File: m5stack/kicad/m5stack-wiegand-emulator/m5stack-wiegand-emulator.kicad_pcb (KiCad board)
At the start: 2 copper layers, 50 x 50 mm, 56 parts, among them J1 2x15 socket header, J2 2x15 pin header, J3 1x5 female, U1 RP2040, U2 ISOW7841, U3 SN74LVC2G126-EP, U4 TPS62906DRL, U5 SN74AHCT1G125

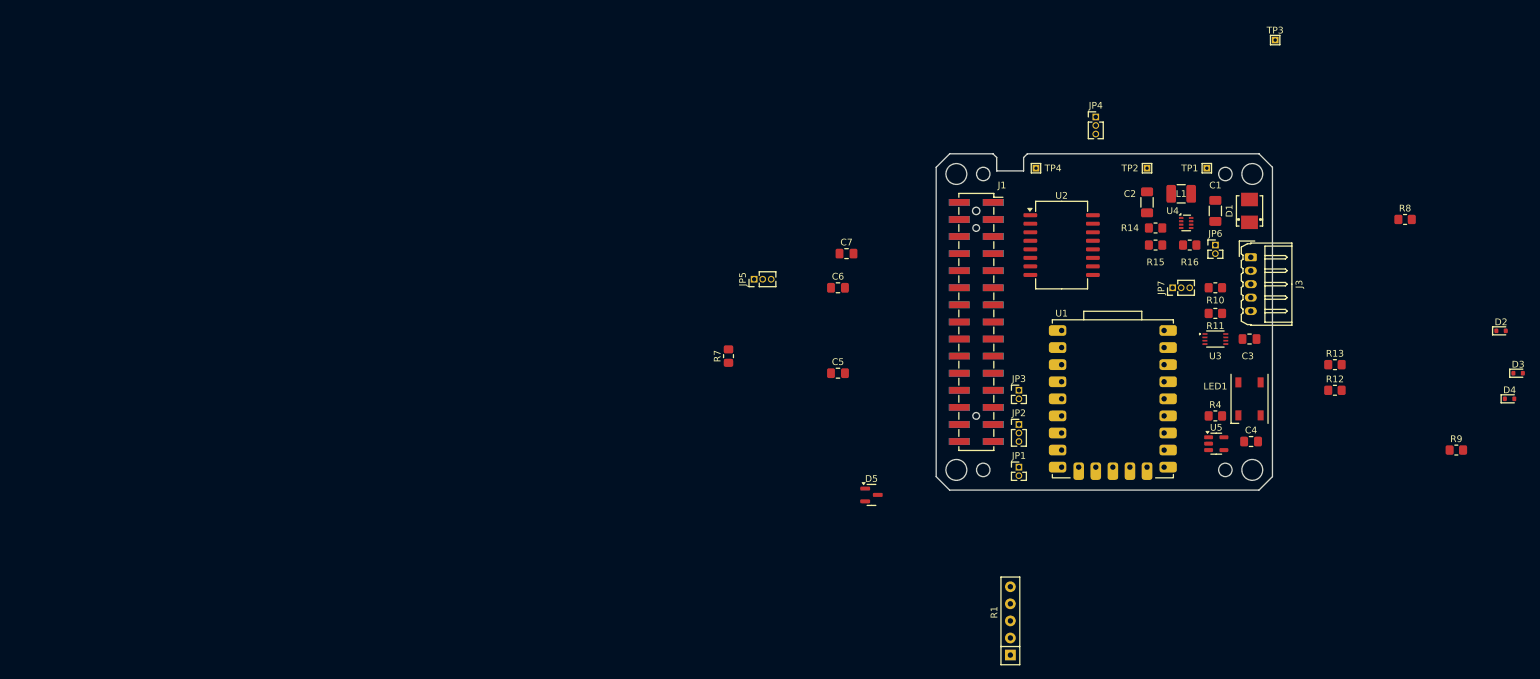
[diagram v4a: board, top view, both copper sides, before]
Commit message: M5: placed all footprints
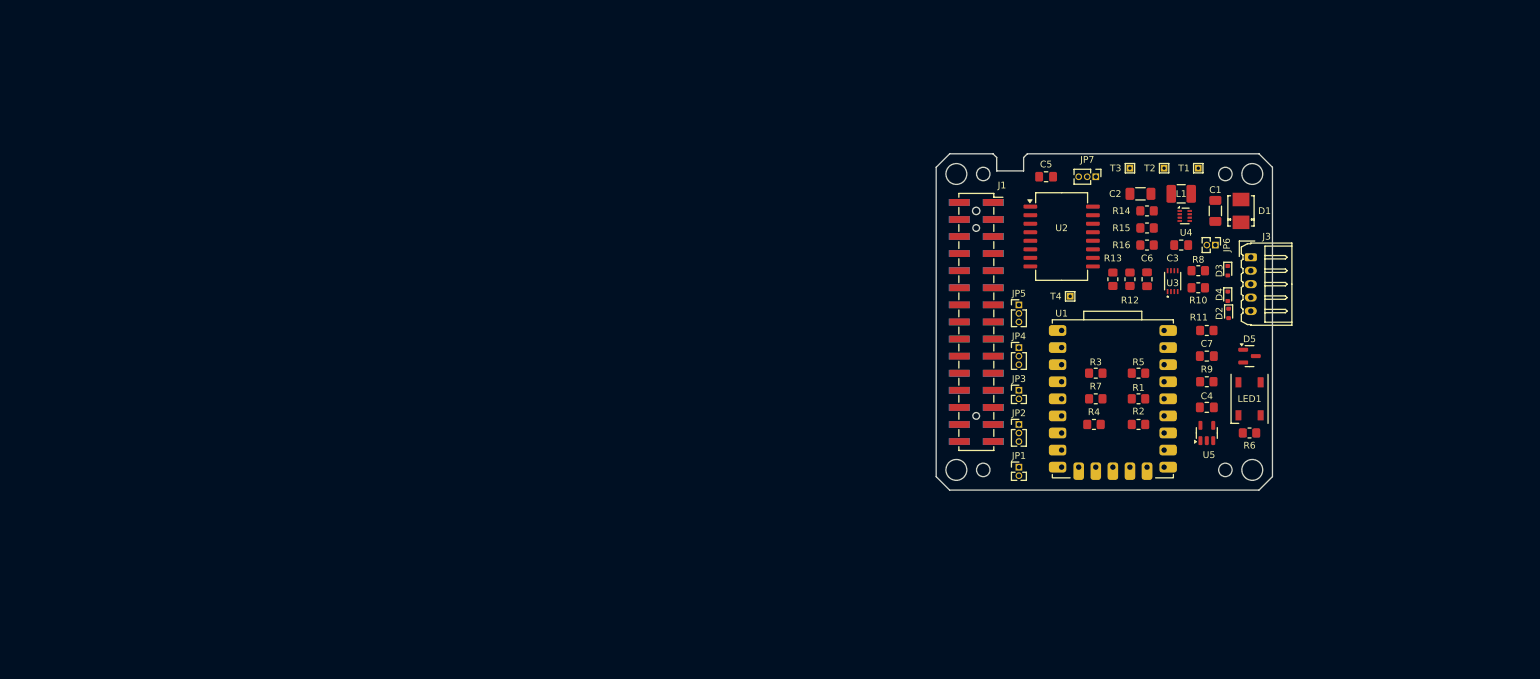
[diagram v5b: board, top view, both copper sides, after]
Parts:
- removed TP1, TP2, TP3, TP4: TestPoint, TestPoint:TestPoint_THTPad_1.0x1.0mm_Drill0.5mm
- added R2: 10k, Resistor_SMD:R_0805_2012Metric_Pad1.20x1.40mm_HandSolder, F.Cu at (119.4, 104.1)
- added R3: 10k, Resistor_SMD:R_0805_2012Metric_Pad1.20x1.40mm_HandSolder, F.Cu at (113.0, 96.5)
- added R5: 10k, Resistor_SMD:R_0805_2012Metric_Pad1.20x1.40mm_HandSolder, F.Cu at (119.4, 96.5)
- added R6: 470, Resistor_SMD:R_0805_2012Metric_Pad1.20x1.40mm_HandSolder, F.Cu at (135.9, 105.4)
- added T1: TestPoint, TestPoint:TestPoint_THTPad_1.0x1.0mm_Drill0.5mm, F.Cu at (128.3, 66.0)
- added T2: TestPoint, TestPoint:TestPoint_THTPad_1.0x1.0mm_Drill0.5mm, F.Cu at (123.2, 66.0)
- added T3: TestPoint, TestPoint:TestPoint_THTPad_1.0x1.0mm_Drill0.5mm, F.Cu at (118.1, 66.0)
- added T4: TestPoint, TestPoint:TestPoint_THTPad_1.0x1.0mm_Drill0.5mm, F.Cu at (109.2, 85.1)
- R1: footprint Resistor_THT:R_Array_SIP5 -> Resistor_SMD:R_0805_2012Metric_Pad1.20x1.40mm_HandSolder
- R4: value 470 -> 10k
- moved D5 59.9 mm to (135.9, 94.0)
- moved C7 55.7 mm to (129.5, 94.0)
- moved R7 55.0 mm to (113.0, 100.3), turned to 0 degrees
- moved C6 46.0 mm to (120.7, 82.5), turned to -90 degrees
- moved D3 45.8 mm to (132.7, 81.3), turned to -90 degrees
- moved D4 44.6 mm to (132.7, 85.1), turned to -90 degrees
- moved R1 42.6 mm to (119.4, 100.3), turned to 0 degrees
- moved C5 42.6 mm to (105.6, 67.3), turned to 180 degrees
- moved D2 40.6 mm to (132.8, 87.6), turned to -90 degrees
- moved JP5 39.6 mm to (101.6, 86.4), turned to 0 degrees
- moved R9 38.5 mm to (129.5, 97.8)
- moved JP4 36.1 mm to (101.6, 92.7)
- moved R13 35.4 mm to (115.6, 82.5), turned to 90 degrees
- moved R12 34.7 mm to (118.1, 82.5), turned to 90 degrees
- moved R8 31.7 mm to (128.3, 81.3)
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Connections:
- R4 pad 1: Net-(U5-Y) -> +3V3
- R4 pad 2: Net-(LED1-DIN) -> Net-(U1-GP14)
- U1 pad 8: Net-(R1C-R3.2) -> Net-(U1-GP15)
- U1 pad 9: Net-(R1D-R4.2) -> Net-(U1-GP14)
- U2 pad 3: Net-(R1C-R3.2) -> Net-(U1-GP15)
- U2 pad 4: Net-(R1D-R4.2) -> Net-(U1-GP14)

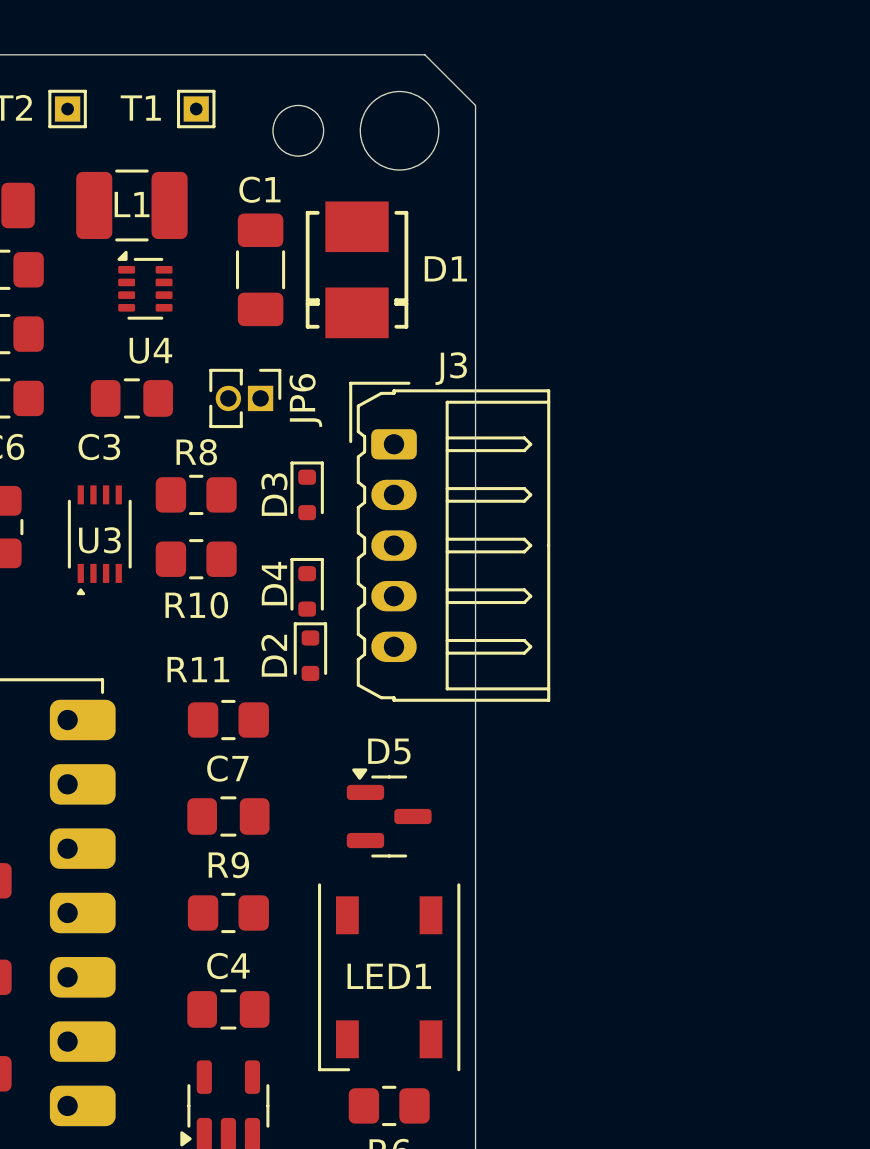
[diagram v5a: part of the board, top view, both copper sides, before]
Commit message: M5: replaced SMD TVS diodes with THT (for hand-soldering)
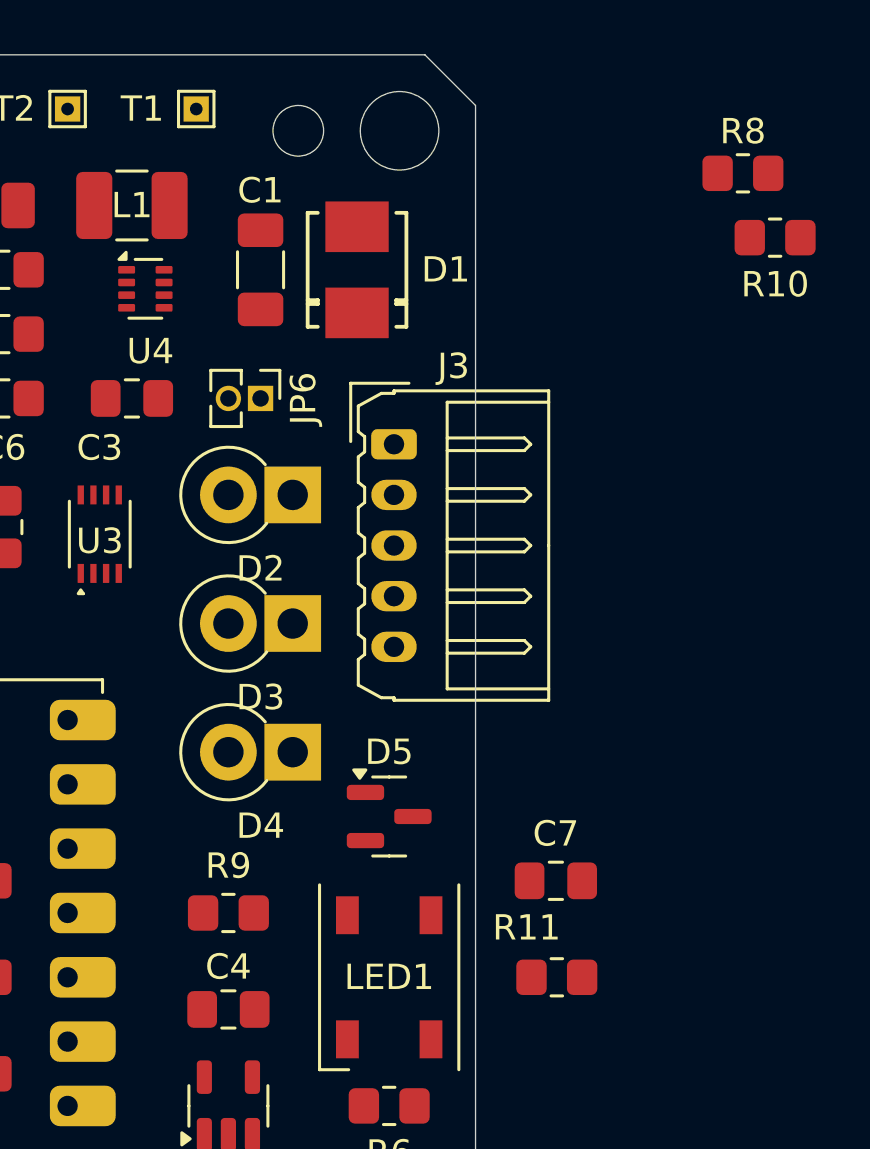
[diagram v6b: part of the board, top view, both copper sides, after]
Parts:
- D2, D3, D4: value D_TVS -> SA5.0A; footprint Diode_SMD:D_SOD-523 -> Diode_THT:D_DO-15_P2.54mm_Vertical_KathodeUp
- moved R10 26.2 mm to (151.1, 71.1)
- moved R8 25.0 mm to (149.9, 68.6)
- moved R11 16.5 mm to (142.5, 100.3)
- moved C7 13.2 mm to (142.5, 96.5)
- moved D2 6.39 mm to (132.1, 81.3), turned to 180 degrees
- moved D4 6.38 mm to (132.1, 91.4), turned to 180 degrees
- moved D3 5.11 mm to (132.1, 86.4), turned to 180 degrees

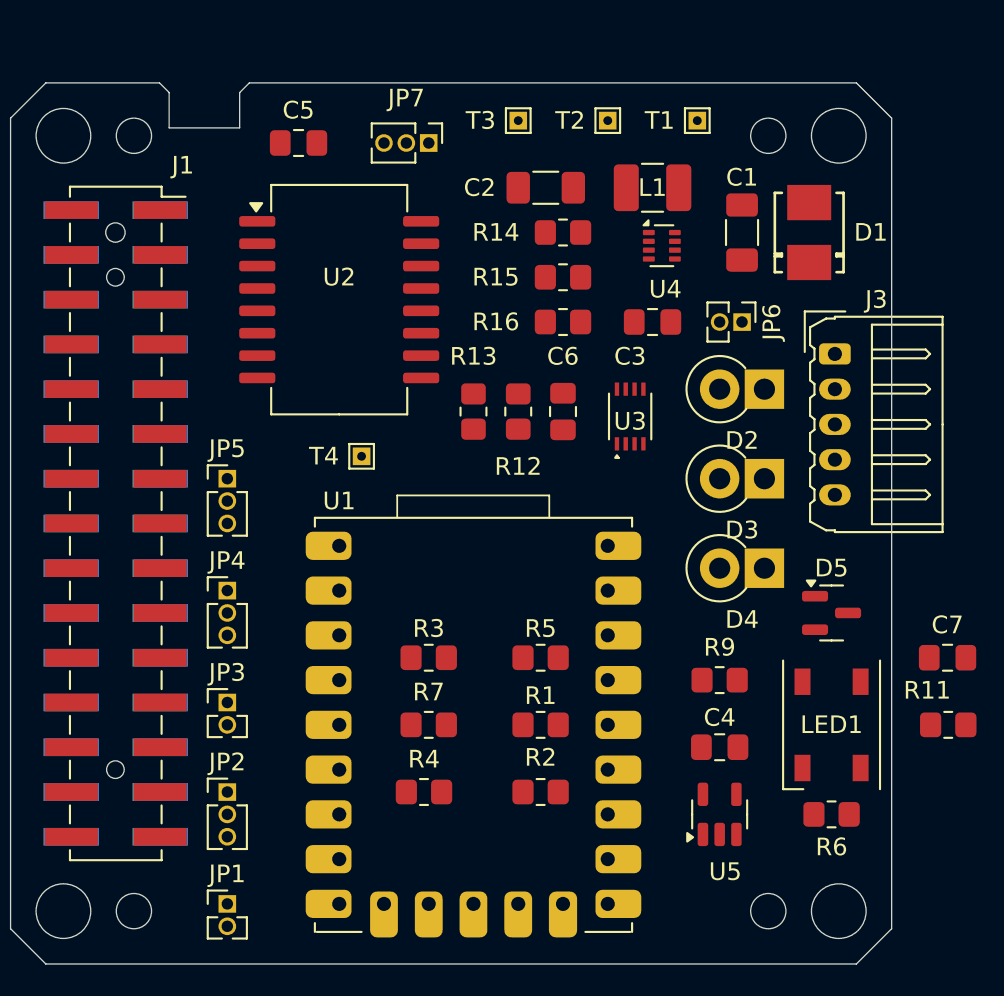
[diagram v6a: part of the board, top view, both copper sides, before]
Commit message: M5: replaced discrete'ish switchmode with module
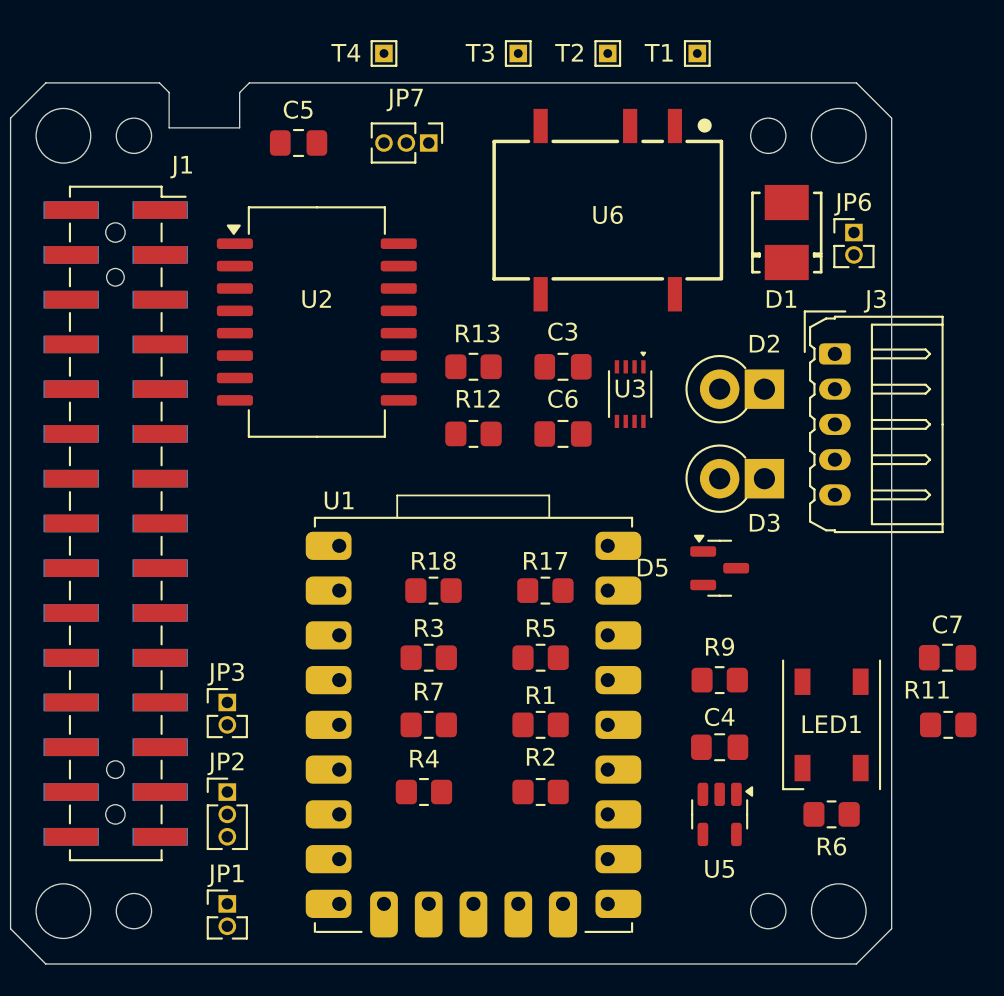
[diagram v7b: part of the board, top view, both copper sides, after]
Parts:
- removed C1: 10uF, Capacitor_SMD:C_1206_3216Metric_Pad1.33x1.80mm_HandSolder
- removed C2: 22uF, Capacitor_SMD:C_1206_3216Metric_Pad1.33x1.80mm_HandSolder
- removed D4: SA5.0A, Diode_THT:D_DO-15_P2.54mm_Vertical_KathodeUp
- removed JP4, JP5: Jumper_3_Bridged12, Connector_PinHeader_1.27mm:PinHeader_1x03_P1.27mm_Vertical
- removed L1: 2.2uH, Inductor_SMD:L_1210_3225Metric_Pad1.42x2.65mm_HandSolder
- removed R14, R15: 100k, Resistor_SMD:R_0805_2012Metric_Pad1.20x1.40mm_HandSolder
- removed R16: 27k, Resistor_SMD:R_0805_2012Metric_Pad1.20x1.40mm_HandSolder
- removed U4: TPS62906DRL, Package_TO_SOT_SMD:SOT-583-8
- added R17: 10k, Resistor_SMD:R_0805_2012Metric_Pad1.20x1.40mm_HandSolder, F.Cu at (119.7, 92.7)
- added R18: 10k, Resistor_SMD:R_0805_2012Metric_Pad1.20x1.40mm_HandSolder, F.Cu at (113.3, 92.7)
- added REF**: M5 Stack 1.1mm reference hole, uhppoted:M5 Stack 1.1mm reference hole, F.Cu at (95.2, 105.4)
- added U6: FISM 1769405241, uhppoted:WPME-FISM_SMT-8_1769205241, F.Cu at (123.2, 71.1)
- moved T4 22.9 mm to (110.5, 62.2)
- moved JP6 8.13 mm to (137.2, 72.4), turned to 0 degrees
- moved D5 6.84 mm to (129.5, 91.4)
- moved C3 5.68 mm to (120.7, 80.0), turned to 180 degrees
- moved T1 3.81 mm to (128.3, 62.2)
- moved T2 3.81 mm to (123.2, 62.2)
- moved T3 3.81 mm to (118.1, 62.2)
- moved R12 2.84 mm to (115.6, 83.8), turned to 0 degrees
- moved R13 2.54 mm to (115.6, 80.0), turned to 0 degrees
- moved U2 1.80 mm to (106.7, 77.5)
- moved D1 1.27 mm to (133.3, 72.4)
- moved C6 1.27 mm to (120.7, 83.8), turned to 0 degrees
- moved U3 1.27 mm to (124.5, 81.6), turned to -90 degrees
- turned U5 to -90 degrees
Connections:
- R1 pad 2: Net-(JP4-C) -> /RXD2
- R2 pad 2: Net-(JP5-C) -> /TXD2
- R5 pad 2: Net-(U1-GP9) -> Net-(U1-GP6)
- R7 pad 1: Net-(U1-GP13) -> Net-(U1-GP10)
- U1 pad 10: Net-(U1-GP13) -> unconnected-(U1-GP13-Pad10)
- U1 pad 13: unconnected-(U1-GP10-Pad13) -> Net-(U1-GP10)
- U1 pad 14: Net-(U1-GP9) -> unconnected-(U1-GP9-Pad14)
- U1 pad 17: unconnected-(U1-GP6-Pad17) -> Net-(U1-GP6)
- U1 pad 18: Net-(JP5-C) -> /TXD2
- U1 pad 19: Net-(JP4-C) -> /RXD2
- U1 pad 22: unconnected-(U1-GP1-Pad22) -> /TXD1
- U1 pad 23: unconnected-(U1-GP0-Pad23) -> /RXD1
- U2 pad 5: Net-(U1-GP13) -> Net-(U1-GP10)
- U5 pad 2: Net-(U1-GP9) -> Net-(U1-GP6)

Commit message: M5: added optional resistors to set drive current for DI/DO
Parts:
- added D4: SA5.0A, Diode_THT:D_DO-15_P2.54mm_Vertical_KathodeUp, F.Cu at (171.4, 86.4)
- added R14: 470, Resistor_SMD:R_0805_2012Metric_Pad1.20x1.40mm_HandSolder, B.Cu at (153.7, 85.1)
- added R15: 470, Resistor_SMD:R_0805_2012Metric_Pad1.20x1.40mm_HandSolder, B.Cu at (153.7, 88.9)
- added R16: 470, Resistor_SMD:R_0805_2012Metric_Pad1.20x1.40mm_HandSolder, B.Cu at (153.7, 92.7)
- added R19: 470, Resistor_SMD:R_0805_2012Metric_Pad1.20x1.40mm_HandSolder, B.Cu at (153.7, 96.5)
- JP2: value Jumper_3_Bridged12 -> Jumper_2_Bridged; footprint Connector_PinHeader_1.27mm:PinHeader_1x03_P1.27mm_Vertical -> Connector_PinHeader_1.27mm:PinHeader_1x02_P1.27mm_Vertical
- JP3: value Jumper_2_Bridged -> Jumper_3_Bridged12; footprint Connector_PinHeader_1.27mm:PinHeader_1x02_P1.27mm_Vertical -> Connector_PinHeader_1.27mm:PinHeader_1x03_P1.27mm_Vertical
- moved JP2 1.27 mm to (101.6, 105.4)
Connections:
- JP2 pad 1: Net-(JP1-B) -> GND
- JP2 pad 2: +5V -> GND
- JP3 pad 1: GND -> Net-(JP1-B)
- JP3 pad 2: GND -> +5V
